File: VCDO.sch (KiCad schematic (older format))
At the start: 93 parts, among them J1 NOTE CV, J10 PROGRAMMING HEADER, J2 MOD CV, J3 WAVE CV, J4 SUB CV, J5 GLIDE TOGGLE, J6 SUB OUT, J7 TEST HEADER, J8 SYNTH POWER, J9 MAIN OUT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

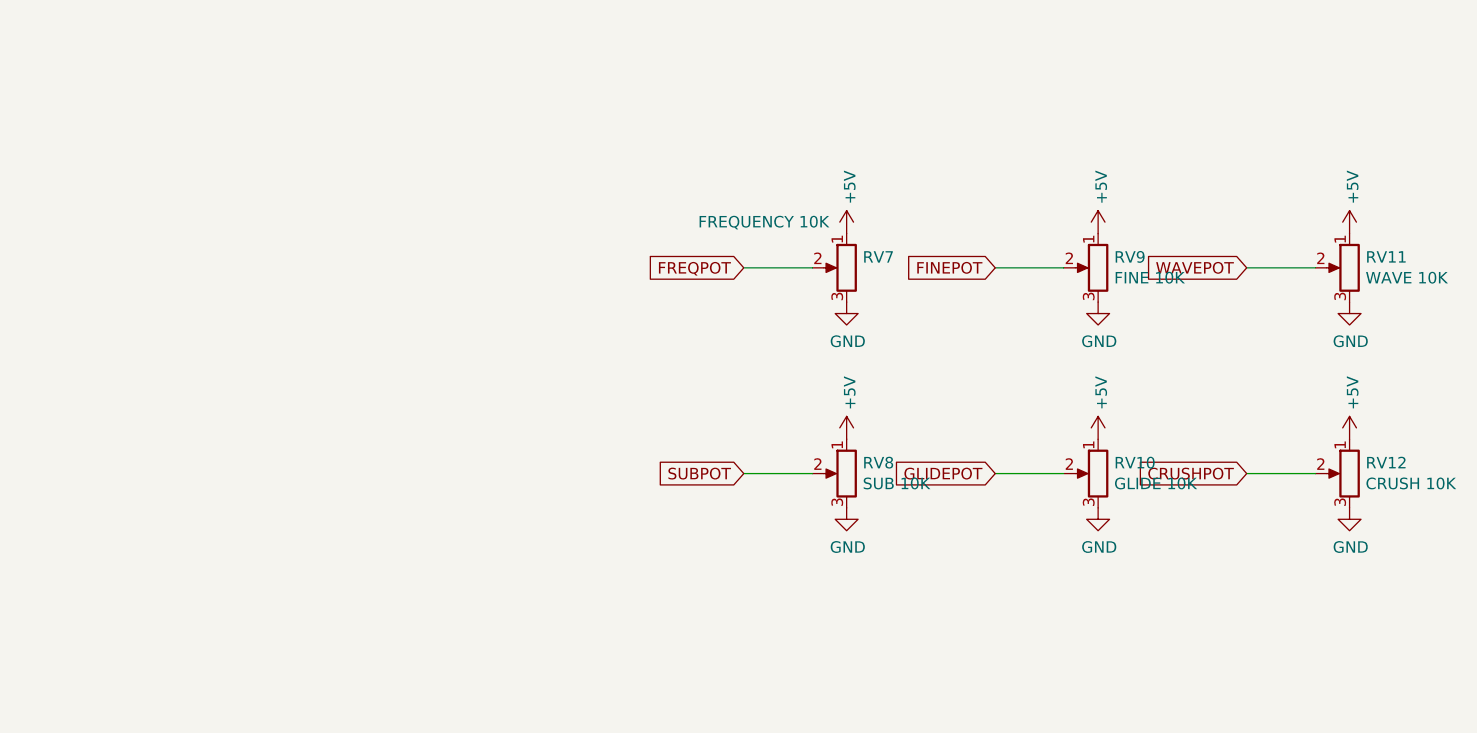
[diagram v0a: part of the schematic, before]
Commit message: add caps again, back to v5
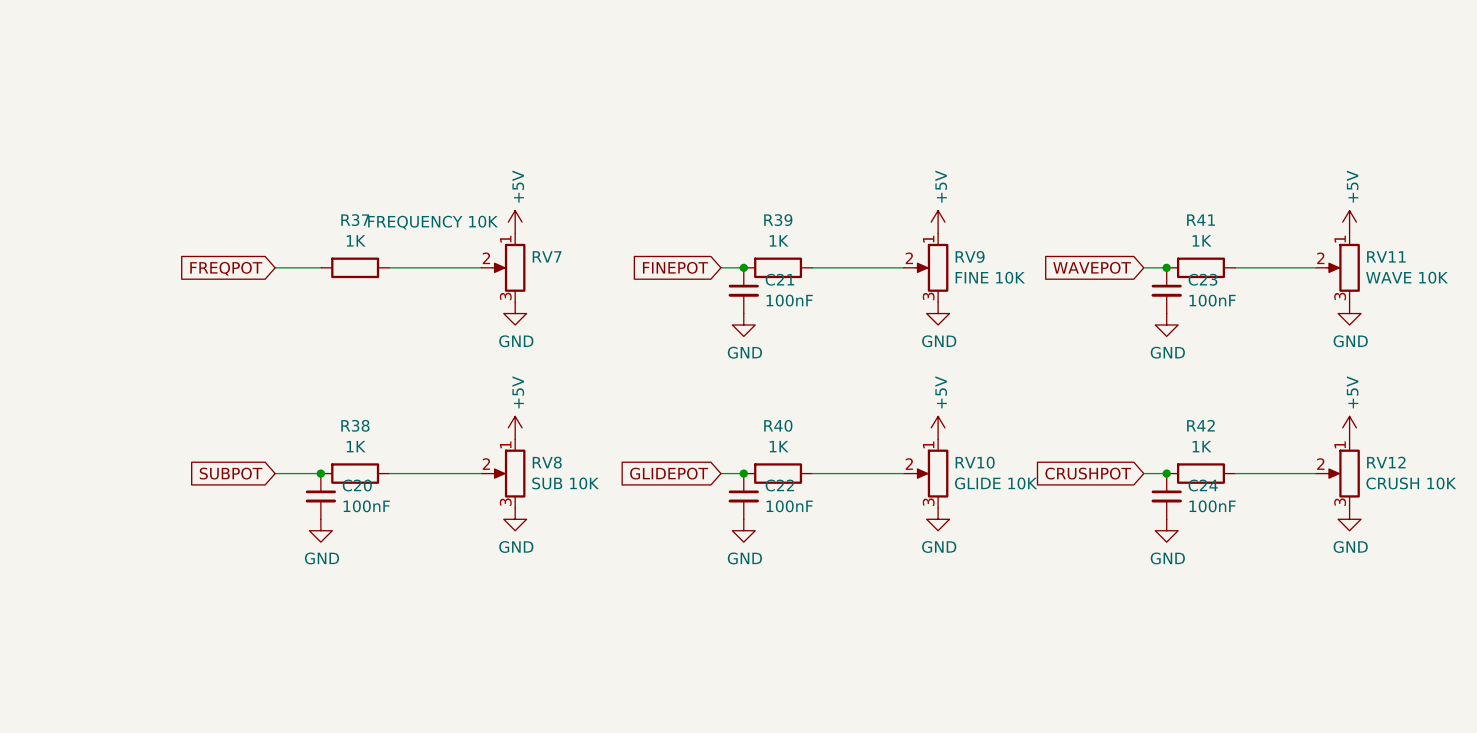
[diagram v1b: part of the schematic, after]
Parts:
- added C20, C21, C22, C23, C24: 100nF, symbol Device:C_Small
- added R37, R38, R39, R40, R41, R42: 1K, symbol Device:R
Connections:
- net CRUSHPOT: now also C24.1, R42.2; no longer RV12.2
- net FINEPOT: now also C21.1, R39.2; no longer RV9.2
- net FREQPOT: now also R37.2; no longer RV7.2
- net GLIDEPOT: now also C22.1, R40.2; no longer RV10.2
- net GND: now also C20.2, C21.2, C22.2, C23.2, C24.2
- net SUBPOT: now also C20.1, R38.2; no longer RV8.2
- net WAVEPOT: now also C23.1, R41.2; no longer RV11.2
- new net: R37.1, RV7.2
- new net: R39.1, RV9.2
- new net: R41.1, RV11.2
- new net: R38.1, RV8.2
- new net: R40.1, RV10.2
- new net: R42.1, RV12.2
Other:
- moved on the sheet: RV10, RV7, RV8, RV9
